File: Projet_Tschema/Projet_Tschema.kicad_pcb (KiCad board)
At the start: 2 copper layers, 58.5 x 48.5 mm, 38 parts, among them J1 Raspberry_Pi_2_3, U1 SC16IS-752, Y1 14.7456M

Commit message: pcb
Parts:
- removed H3: Conn_01x08, Connector_PinHeader_2.54mm:PinHeader_2x04_P2.54mm_Vertical
- removed H5: Conn_01x05, Connector_PinHeader_2.54mm:PinHeader_1x05_P2.54mm_Vertical
- removed R6, R7: 10K, Resistor_SMD:R_0805_2012Metric
- added C4: 10uF, Capacitor_SMD:C_0805_2012Metric, F.Cu at (162.6, 95.2)
- added C5: 10uF, Capacitor_SMD:C_0805_2012Metric, F.Cu at (167.6, 95.2)
- added D2: LED_Filled, LED_SMD:LED_0805_2012Metric, F.Cu at (172.7, 106.3)
- added J2: Screw_Terminal_01x02, Connector_PinHeader_2.54mm:PinHeader_1x02_P2.54mm_Vertical, F.Cu at (163.8, 109.2)
- added J3: Conn_D42V55F5, Connector_PinHeader_2.54mm:PinHeader_2x06_P2.54mm_Vertical, F.Cu at (179.1, 110.5)
- added R24: 1K, Resistor_SMD:R_0805_2012Metric, F.Cu at (172.7, 102.5)
- added U2: AMS1117, Package_TO_SOT_SMD:SOT-223-3_TabPin2, F.Cu at (165.1, 101.6)
- moved Y1 68.4 mm to (153.7, 109.2)
- moved R15 64.5 mm to (144.1, 105.4), turned to 180 degrees
- moved L_TXB1 64.0 mm to (174.0, 84.7)
- moved R4 63.7 mm to (139.3, 99.1), turned to 180 degrees
- moved J1 63.3 mm to (128.3, 118.9)
- moved R10 63.0 mm to (174.0, 89.8)
- moved R19 62.3 mm to (144.1, 110.5), turned to 180 degrees
- moved R5 61.5 mm to (133.3, 89.8)
- moved L_RXA1 61.4 mm to (133.3, 84.7)
- moved H2 61.4 mm to (162.6, 85.1)
- moved R8 61.2 mm to (129.5, 89.8)
- moved R11 61.2 mm to (144.1, 102.9), turned to 180 degrees
- moved L_TXA1 61.2 mm to (129.5, 84.7)
- moved C1 61.1 mm to (144.4, 99.1), turned to 180 degrees
- moved R16 59.1 mm to (140.3, 105.4), turned to 180 degrees
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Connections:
- net A1 renamed /A1
- net AO renamed /A0
- net CTSA renamed /CTSA
- net CTSB renamed /CTSB
- net IRQ renamed /IRQ
- net P SCL renamed /P_SCL
- net P SDA renamed /P_SDA
- net P20 renamed /P20
- net P21 renamed /P21
- net P22 renamed /P22
- net P23 renamed /P23
- net P24 renamed /P24
- net RTSA renamed /RTSA
- net RTSB renamed /RTSB
- net RXDA renamed /RXDA
- net RXDB renamed /RXDB
- net TXDA renamed /TXDA
- net TXDB renamed /TXDB
- C1 pad 2: +3.3V -> /3V3
- H1 pad 1: 3.3V -> /3V3
- H2 pad 1: 3.3V -> /3V3
- J1 pad 1: 3.3V -> unconnected-(J1-3V3-Pad1)
- J1 pad 17: 3.3V -> unconnected-(J1-3V3-Pad17)
- J1 pad 2: unconnected-(J1-5V-Pad2) -> /5V
- J1 pad 27: unconnected-(J1-SDA0-Pad27) -> /&lt;NO NET&gt;
- J1 pad 4: unconnected-(J1-5V-Pad4) -> /5V
- R1 pad 1: +3.3V -> /3V3
- R10 pad 1: +3.3V -> /3V3
- R11 pad 2: 3.3V -> /3V3
- R12 pad 1: 3.3V -> /3V3
- R2 pad 1: +3.3V -> /3V3
- R3 pad 1: +3.3V -> /3V3
- R4 pad 1: +3.3V -> /3V3
- R5 pad 1: +3.3V -> /3V3
- R8 pad 1: +3.3V -> /3V3
- R9 pad 1: +3.3V -> /3V3
- U1 pad 18: GPIO0 -> unconnected-(U1-GPIO0/~{DSRB}-Pad18)
- U1 pad 19: GPIO1 -> unconnected-(U1-GPIO1/~{DTRB}-Pad19)
- U1 pad 20: GPIO2 -> unconnected-(U1-GPIO2/~{CDB}-Pad20)
- U1 pad 21: GPIO3 -> unconnected-(U1-GPIO3/~{RIB}-Pad21)
- U1 pad 25: GPIO4 -> unconnected-(U1-GPIO4/~{DSRA}-Pad25)
- U1 pad 26: GPIO5 -> unconnected-(U1-GPIO5/~{DTRA}-Pad26)
- U1 pad 27: GPIO6 -> unconnected-(U1-GPIO6/~{CDA}-Pad27)
- U1 pad 28: GPIO7 -> unconnected-(U1-GPIO7/~{RIA}-Pad28)
- U1 pad 8: +3.3V -> /3V3
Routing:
- net 3.3V: track 130.5 -> 0.00 mm, vias 6 -> 0
- net +3.3V: track 85.1 -> 0.00 mm, vias 3 -> 0
- net /P_SDA: track 76.5 -> 0.00 mm, vias 4 -> 0
- net /IRQ: track 73.4 -> 0.00 mm, vias 2 -> 0
- net /P_SCL: track 72.8 -> 0.00 mm, vias 4 -> 0
- net /TXDA: track 53.1 -> 0.00 mm, vias 3 -> 0
- net /RXDA: track 47.1 -> 0.00 mm, vias 3 -> 0
- net /RXDB: track 38.3 -> 0.00 mm, vias 2 -> 0
- net /TXDB: track 35.7 -> 0.00 mm, vias 2 -> 0
- net GND: track 27.5 -> 0.00 mm, vias 7 -> 0
- net /RTSB: track 26.0 -> 0.00 mm, vias 2 -> 0
- net /CTSB: track 25.7 -> 0.00 mm, vias 2 -> 0
- net /CTSA: track 23.5 -> 0.00 mm, vias 3 -> 0
- net /RTSA: track 22.9 -> 0.00 mm, vias 3 -> 0
- net Net-(U1-I2C/~{SPI}): track 22.2 -> 0.00 mm, vias 3 -> 0
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- added copper zone on B.Cu, net (none)
- added copper zone on F.Cu, net (none)
- removed copper zone on B.Cu, net GND
- removed copper zone on F.Cu, net GND
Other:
- board outline removed

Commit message: first version finished
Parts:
- removed D2: LED_Filled, LED_SMD:LED_0805_2012Metric
- removed R14, R15, R16, R17, R18, R19, R20, R21, R22, R23: NC, Resistor_SMD:R_0805_2012Metric
- removed R24: 1K, Resistor_SMD:R_0805_2012Metric
- Y1: footprint Crystal:Crystal_SMD_3225-4Pin_3.2x2.5mm -> Crystal:Crystal_HC52-U_Vertical
- moved J1 48.3 mm to (175.6, 109.6), turned to -90 degrees
- moved R3 34.4 mm to (173.1, 103.0), turned to -90 degrees
- moved D1 32.4 mm to (152.1, 86.2)
- moved R1 32.4 mm to (152.1, 90.0)
- moved C1 28.7 mm to (173.1, 98.9), turned to -90 degrees
- moved Y1 19.6 mm to (135.5, 101.7)
- moved J2 17.4 mm to (180.7, 105.0), turned to -90 degrees
- moved C4 10.7 mm to (170.1, 102.9), turned to -90 degrees
- moved J3 10.2 mm to (180.7, 100.5)
- moved R4 9.00 mm to (130.4, 97.8), turned to 90 degrees
- moved L_RXA1 7.33 mm to (129.9, 91.2), turned to 90 degrees
- moved L_TXA1 7.33 mm to (133.0, 91.2), turned to 90 degrees
- moved L_TXB1 6.24 mm to (173.1, 90.9), turned to 90 degrees
- moved L_RXB1 6.19 mm to (170.6, 90.9), turned to 90 degrees
- moved C2 5.06 mm to (141.2, 97.9), turned to 0 degrees
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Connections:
- H1 pad 5: /RTSA -> unconnected-(H1-Pin_5-Pad5)
- H1 pad 6: /CTSA -> unconnected-(H1-Pin_6-Pad6)
- H2 pad 5: /RTSB -> unconnected-(H2-Pin_5-Pad5)
- H2 pad 6: /CTSB -> unconnected-(H2-Pin_6-Pad6)
- J1 pad 15: /P22 -> unconnected-(J1-GPIO3-Pad15)
- J1 pad 16: /P23 -> unconnected-(J1-GPIO4-Pad16)
- J1 pad 38: /P20 -> unconnected-(J1-GPIO28-Pad38)
- J1 pad 40: /P21 -> unconnected-(J1-GPIO29-Pad40)
- J3 pad 1: Net-(J3-Pin_1) -> unconnected-(J3-Pin_1-Pad1)
- J3 pad 11: GND -> /5V
- J3 pad 3: /Vin -> unconnected-(J3-Pin_3-Pad3)
- J3 pad 4: GND -> unconnected-(J3-Pin_4-Pad4)
- J3 pad 5: GND -> /Vin
- J3 pad 6: /5V -> /Vin
- J3 pad 7: unconnected-(J3-Pin_7-Pad7) -> GND
- J3 pad 8: unconnected-(J3-Pin_8-Pad8) -> GND
- J3 pad 9: /Vin -> GND
- U1 pad 1: /RTSA -> unconnected-(U1-~{RTSA}-Pad1)
- U1 pad 16: /CTSB -> unconnected-(U1-~{CTSB}-Pad16)
- U1 pad 17: /RTSB -> unconnected-(U1-~{RTSB}-Pad17)
- U1 pad 2: /CTSA -> unconnected-(U1-~{CTSA}-Pad2)
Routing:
- net /3V3: track 0.00 -> 146.3 mm, vias 0 -> 4
- net /5V: track 0.00 -> 67.8 mm, vias 0 -> 1
- net /IRQ: track 0.00 -> 50.0 mm
- net /P24: track 0.00 -> 46.1 mm
- net /TXDB: track 0.00 -> 36.8 mm
- net /RXDA: track 0.00 -> 35.8 mm
- net /P_SCL: track 0.00 -> 34.4 mm, vias 0 -> 2
- net /P_SDA: track 0.00 -> 32.2 mm, vias 0 -> 2
- net /TXDA: track 0.00 -> 24.1 mm
- net /RXDB: track 0.00 -> 23.6 mm
- net GND: track 0.00 -> 21.2 mm, vias 0 -> 4
- net Net-(U1-I2C/~{SPI}): track 0.00 -> 20.2 mm, vias 0 -> 2
- net /Vin: track 0.00 -> 17.0 mm
- net Net-(U1-XTAL2): track 0.00 -> 15.0 mm
- net Net-(U1-XTAL1): track 0.00 -> 14.8 mm
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- added copper zone on B.Cu, net GND
- added copper zone on F.Cu, net GND
- removed copper zone on B.Cu, net (none)
- removed copper zone on F.Cu, net (none)
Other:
- board outline added: 65 x 33.5 mm

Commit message: routes updated
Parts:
- added J4: DRF0571_Vin-, Connector_PinHeader_2.54mm:PinHeader_1x01_P2.54mm_Vertical, F.Cu at (180.3, 103.9)
- added J5: DRF0571_Vin, Connector_PinHeader_2.54mm:PinHeader_1x01_P2.54mm_Vertical, F.Cu at (193.3, 103.9)
- added J6: DRF0571_Vout-, Connector_PinHeader_2.54mm:PinHeader_1x01_P2.54mm_Vertical, F.Cu at (193.5, 85.1)
- J3: value Conn_D42V55F5 -> DRF0571_Vout; footprint Connector_PinHeader_2.54mm:PinHeader_2x06_P2.54mm_Vertical -> Connector_PinHeader_2.54mm:PinHeader_1x01_P2.54mm_Vertical
- moved J3 15.4 mm to (180.3, 85.1), turned to 0 degrees
- moved J2 7.73 mm to (185.9, 110.7), turned to 90 degrees
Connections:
- J3 pad 1: unconnected-(J3-Pin_1-Pad1) -> /5V
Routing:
- net /5V: track 67.8 -> 58.1 mm
- net /Vin: track 17.0 -> 8.86 mm
- net /IRQ: track 50.0 -> 52.1 mm
- net /RXDA: track 35.8 -> 37.3 mm
- net /3V3: track 146.3 -> 147.7 mm
- net /P24: track 46.1 -> 47.4 mm
- net /A1: track 8.45 -> 9.19 mm
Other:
- board size 65 x 33.5 mm -> 74.7 x 33.5 mm

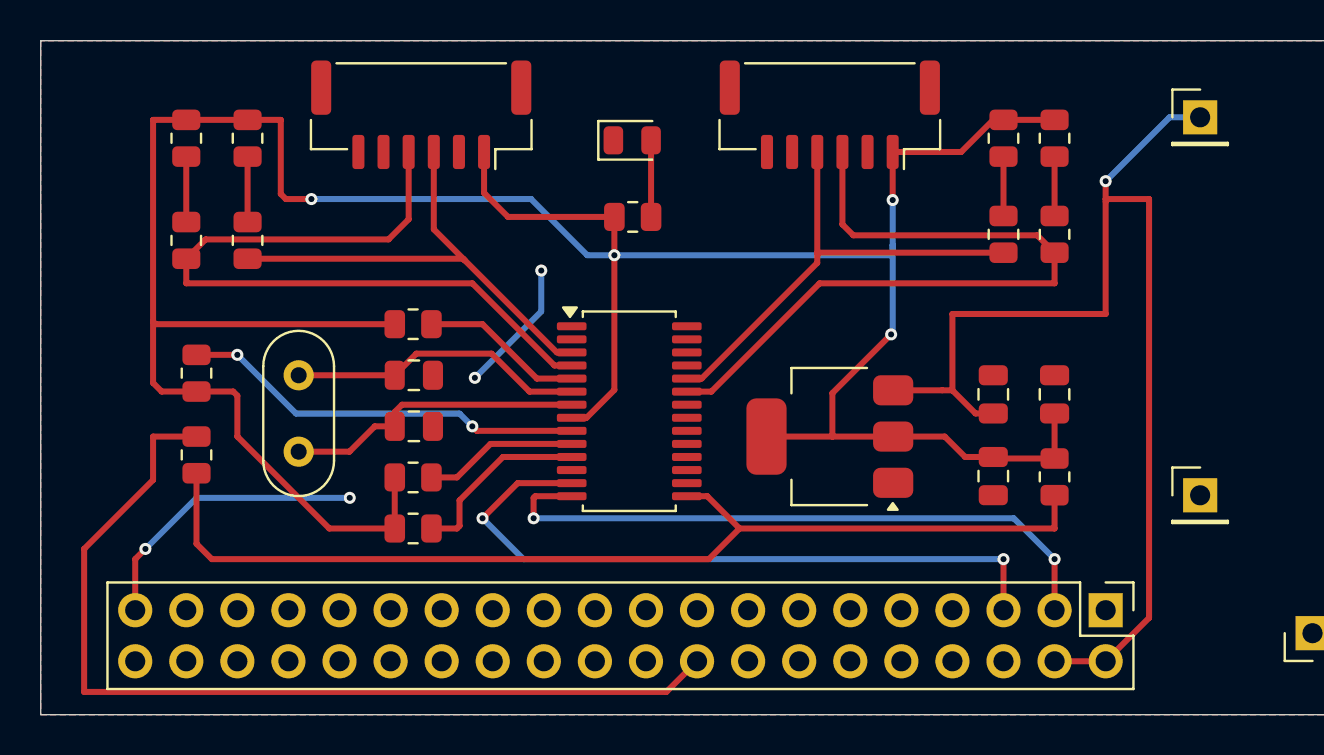
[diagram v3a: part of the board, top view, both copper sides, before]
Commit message: Final adjustments for gerber generation
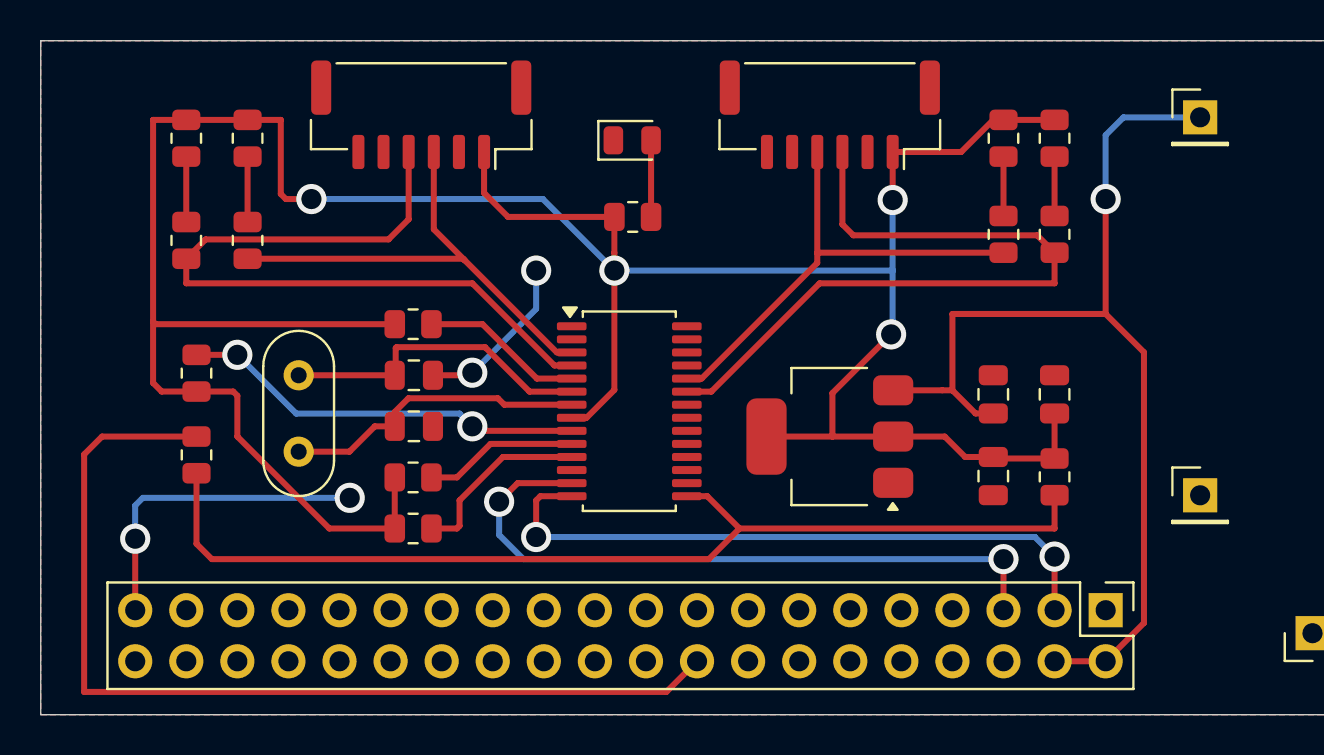
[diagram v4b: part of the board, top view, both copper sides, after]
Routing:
- net /5V: track 58.1 -> 52.2 mm
- net GND: track 21.2 -> 24.4 mm
- net /P24: track 47.4 -> 48.9 mm
- net Net-(U1-XTAL1): track 14.8 -> 15.8 mm
- net /P_SCL: track 34.4 -> 33.8 mm
